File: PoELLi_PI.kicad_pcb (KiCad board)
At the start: 2 copper layers, 85 x 56 mm, 14 parts, among them J1 RJ45, J2 RJ45, P1 CONN_02X20

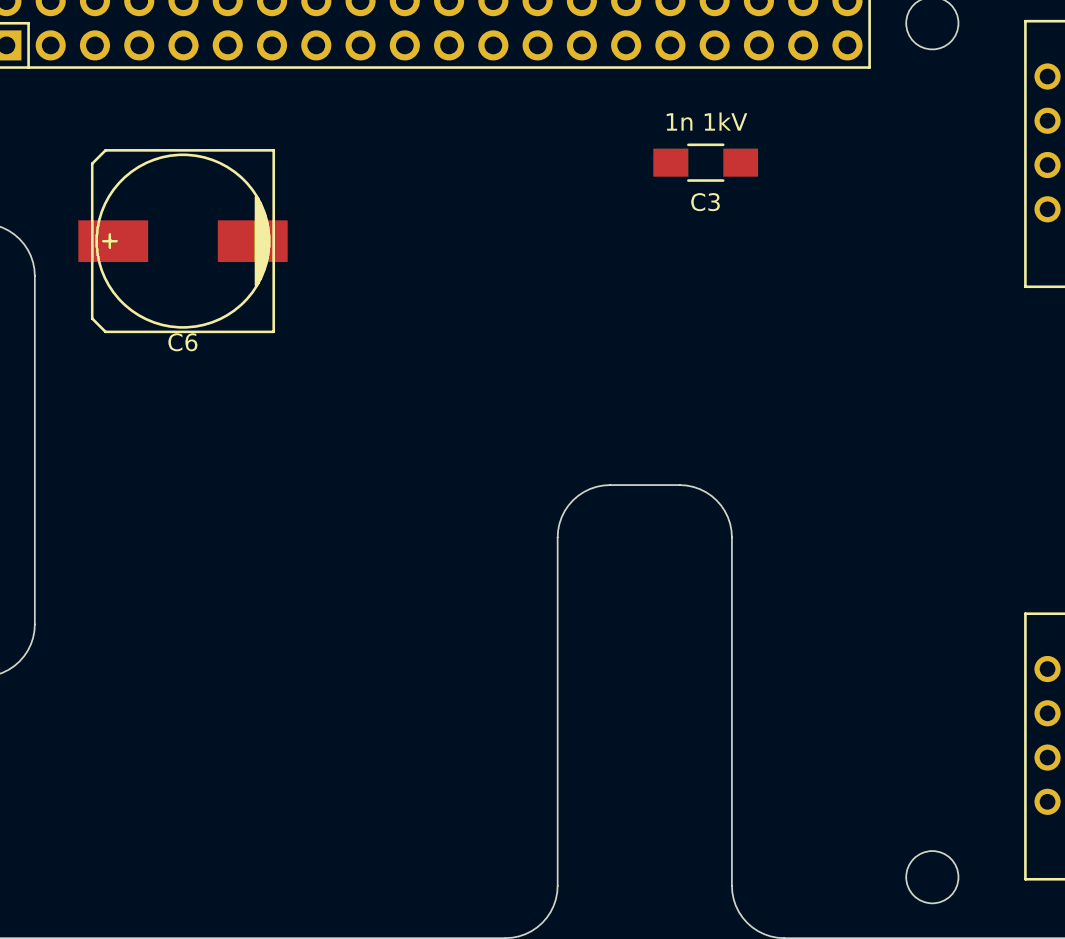
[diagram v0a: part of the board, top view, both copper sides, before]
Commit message: Add input protection diode
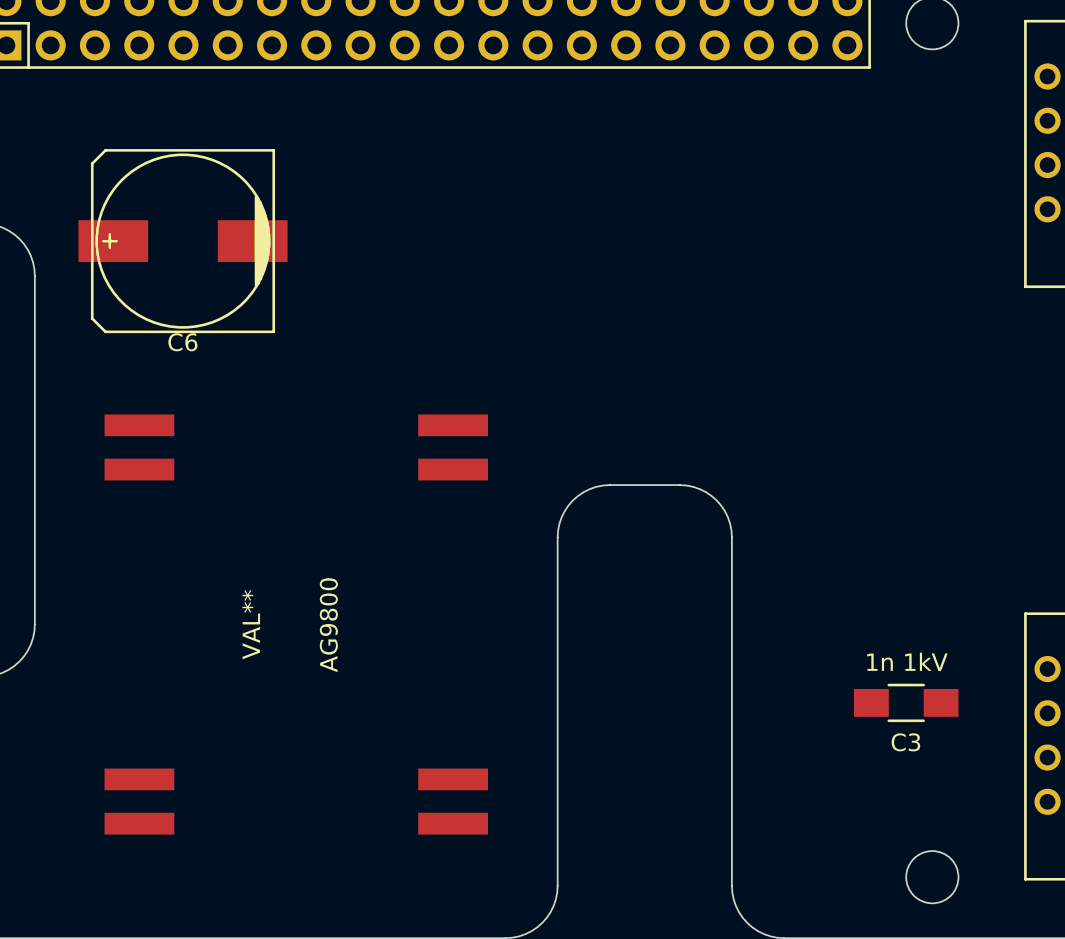
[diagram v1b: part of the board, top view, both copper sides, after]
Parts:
- added AG9800: VAL**, AG9800, F.Cu at (60.0, 70.0)
- moved C3 33.1 mm to (95.0, 74.5)
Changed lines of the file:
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@@
     (links 25)
     (no_connects 22)
-    (area 34.949999 31.949999 120.050001 88.050001)
+    (area 25.000001 25.65 194.729001 108.429)
     (thickness 1.6)
-    (drawings 40)
+    (drawings 41)
     (tracks 0)
     (zones 0)
-    (modules 14)
+    (modules 15)
     (nets 56)
   )
@@
     (mod_text_size 1 1)
     (mod_text_width 0.15)
-    (pad_size 1.5 1.5)
-    (pad_drill 0.6)
+    (pad_size 1.25 4)
+    (pad_drill 0)
     (pad_to_mask_clearance 0)
     (aux_axis_origin 0 0)
@@
     (add_net "Net-(P1-Pad8)")
   )
+  (module AG9800 (layer F.Cu)
+    (at 60 70 270)
+    (fp_text reference AG9800 (at 0 -1.905 270) (layer F.SilkS)
+      (effects (font (size 1 1) (thickness 0.15)))
+    )
+    (fp_text value VAL** (at 0 2.54 270) (layer F.SilkS)
+      (effects (font (size 1 1) (thickness 0.15)))
+    )
+    (pad 8 smd rect (at -11.43 -9 270) (size 1.25 4) (layers F.Cu F.Paste F.Mask))
+    (pad 7 smd rect (at -8.89 -9 270) (size 1.25 4) (layers F.Cu F.Paste F.Mask))
+    (pad 5 smd rect (at 11.43 -9 270) (size 1.25 4) (layers F.Cu F.Paste F.Mask))
+    (pad 6 smd rect (at 8.89 -9 270) (size 1.25 4) (layers F.Cu F.Paste F.Mask))
+    (pad 3 smd rect (at 8.89 9 270) (size 1.25 4) (layers F.Cu F.Paste F.Mask))
+    (pad 4 smd rect (at 11.43 9 270) (size 1.25 4) (layers F.Cu F.Paste F.Mask))
+    (pad 2 smd rect (at -8.89 9 270) (size 1.25 4) (layers F.Cu F.Paste F.Mask))
+    (pad 1 smd rect (at -11.43 9 270) (size 1.25 4) (layers F.Cu F.Paste F.Mask))
+  )
   (module Pin_Headers:Pin_Header_Straight_2x20 (layer F.Cu)
     (at 169 79.5)
@@
   )
   (module Capacitors_SMD:C_1206_HandSoldering (layer F.Cu)
-    (at 83.5 43.5 180)
+    (at 95 74.5 180)
     (descr "Capacitor SMD 1206, hand soldering")
     (tags "capacitor 1206")
@@
     )
   )
+  (gr_line (start 85.5 65) (end 74.5 65) (angle 90) (layer Dwgs.User) (width 0.2))
   (dimension 29 (width 0.3) (layer Dwgs.User)
     (gr_text "29.000 mm" (at 53 27.15) (layer Dwgs.User)

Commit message: First functional version before cosmetic changes
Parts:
- removed AG9800: VAL**, AG9800
- added B2: MB110S, project_specific:TO-269AA, F.Cu at (82.5, 43.0)
- added C10: 10n, Capacitors_SMD:C_0603_HandSoldering, F.Cu at (52.5, 72.2)
- added C11: 10u, Capacitors_SMD:C_0603_HandSoldering, F.Cu at (51.0, 72.2)
- added C7: 4n7 2kV, Capacitors_SMD:C_1812_HandSoldering, F.Cu at (69.8, 54.6)
- added C8: 4n7 2kV, Capacitors_SMD:C_1812_HandSoldering, F.Cu at (62.6, 47.5)
- added C9: 4n7 2kV, Capacitors_SMD:C_1812_HandSoldering, F.Cu at (59.7, 54.6)
- added D1: SMA58, Diodes_SMD:Diode-SMA_Handsoldering, F.Cu at (71.0, 49.5)
- added D2: LED, Resistors_SMD:R_0603_HandSoldering, F.Cu at (46.8, 75.3)
- added F1: FUSE, Resistors_SMD:R_0603_HandSoldering, F.Cu at (43.2, 43.2)
- added FB1: FILTER, Resistors_SMD:R_0603_HandSoldering, F.Cu at (77.5, 55.5)
- added FB2: FILTER, Resistors_SMD:R_0603_HandSoldering, F.Cu at (75.5, 44.5)
- added FB3: FILTER, Resistors_SMD:R_0603_HandSoldering, F.Cu at (77.5, 51.5)
- added FB4: FILTER, Resistors_SMD:R_0603_HandSoldering, F.Cu at (79.5, 51.5)
- added FB5: FILTER, Resistors_SMD:R_0603_HandSoldering, F.Cu at (71.5, 44.5)
- added FB6: FILTER, Resistors_SMD:R_0603_HandSoldering, F.Cu at (71.5, 42.5)
- added FB7: FILTER, Resistors_SMD:R_0603_HandSoldering, F.Cu at (77.5, 47.5)
- added FB8: FILTER, Resistors_SMD:R_0603_HandSoldering, F.Cu at (67.0, 44.5)
- added R5: 180R, Resistors_SMD:R_0603_HandSoldering, F.Cu at (46.2, 72.2)
- added R6: 100R 250 mW, Resistors_SMD:R_0603_HandSoldering, F.Cu at (47.9, 72.2)
- added R7: 100R 250 mW, Resistors_SMD:R_0603_HandSoldering, F.Cu at (49.5, 72.2)
- added TR1: 749012011, project_specific:WE_749012011, F.Cu at (104.0, 60.0)
- added U1: AG9800, AG9800, F.Cu at (62.2, 72.4)
- B1: value MBS1 -> MB110S; footprint Pin_Headers:Pin_Header_Straight_2x20 -> project_specific:TO-269AA
- C3: value 1n 1kV -> 1n 2kV
- J1, J2: footprint Connect:RJ45_8 -> project_specific:SS-7188S-A-NF
- moved B1 89.1 mm to (82.5, 58.0), turned to 270 degrees
- moved C1 60.4 mm to (92.5, 45.5), turned to 180 degrees
- moved C2 57.1 mm to (92.5, 43.0), turned to 180 degrees
- moved R2 56.1 mm to (88.5, 43.0), turned to 180 degrees
- moved R1 53.7 mm to (88.5, 45.5), turned to 180 degrees
- moved C5 45.1 mm to (92.5, 55.5), turned to 180 degrees
- moved R4 43.9 mm to (88.5, 55.5), turned to 180 degrees
- moved C4 42.8 mm to (92.5, 58.0), turned to 180 degrees
- moved R3 41.5 mm to (88.5, 58.0), turned to 180 degrees
- moved C3 24.6 mm to (89.5, 50.5), turned to 0 degrees
- moved C6 2.33 mm to (51.5, 46.8)
- moved J1 1.13 mm to (111.8, 78.1)
- moved J2 1.12 mm to (111.8, 41.9)
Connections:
- C6 pad 1: +5V -> /AG_OUT_+
- J1 pad 1: Net-(J1-Pad1) -> /TD+
- J1 pad 2: Net-(J1-Pad2) -> /TD-
- J1 pad 3: Net-(J1-Pad3) -> /RD+
- J1 pad 6: Net-(J1-Pad6) -> /RD-
- J2 pad 1: Net-(J2-Pad1) -> /TX+
- J2 pad 2: Net-(J2-Pad2) -> /TX-
- J2 pad 3: Net-(J2-Pad3) -> /RX+
- J2 pad 6: Net-(J2-Pad6) -> /RX-
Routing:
- net /AG_IN_+: track 0.00 -> 86.8 mm, vias 0 -> 6
- net /AG_IN_-: track 0.00 -> 66.4 mm, vias 0 -> 6
- net /VIN: track 0.00 -> 35.0 mm
- net Net-(C3-Pad1): track 0.00 -> 30.3 mm, vias 0 -> 3
- net GND: track 0.00 -> 28.5 mm, vias 0 -> 5
- net /POE_A-: track 0.00 -> 28.2 mm
- net GNDD: track 0.00 -> 27.1 mm
- net /AG_OUT_+: track 0.00 -> 24.1 mm
- net /POE_B+: track 0.00 -> 23.5 mm
- net /POE_B-: track 0.00 -> 22.6 mm
- net /TD+: track 0.00 -> 20.7 mm
- net /TD-: track 0.00 -> 20.1 mm
- net /RX-: track 0.00 -> 19.6 mm
- net /RD+: track 0.00 -> 19.4 mm
- net /POE_A+: track 0.00 -> 18.5 mm
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- added copper zone on F.Cu, net +5V
- added copper zone on B.Cu, net /AG_IN_+
- added copper zone on F.Cu, net /AG_IN_+
- added copper zone on B.Cu, net /AG_IN_-
- added copper zone on F.Cu, net /AG_IN_-
- added copper zone on F.Cu, net /AG_OUT_+
- added copper zone on B.Cu, net GND
- added copper zone on F.Cu, net GND
- added copper zone on B.Cu, net GNDA
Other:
- net class Default: clearance 0.254 -> 0.199
- net class Ethernet Signal added: clearance 0.199, trace_width 0.6, via_dia 0.889, via_drill 0.635
- net class Ethernet shield added: clearance 0.399, trace_width 0.254, via_dia 0.889, via_drill 0.635
- rule trace_clearance: 0.254 -> 0.199
- rule trace_min: 0.254 -> 0.15
- rule via_min_drill: 0.508 -> 0.3
- rule via_min_size: 0.889 -> 0.6

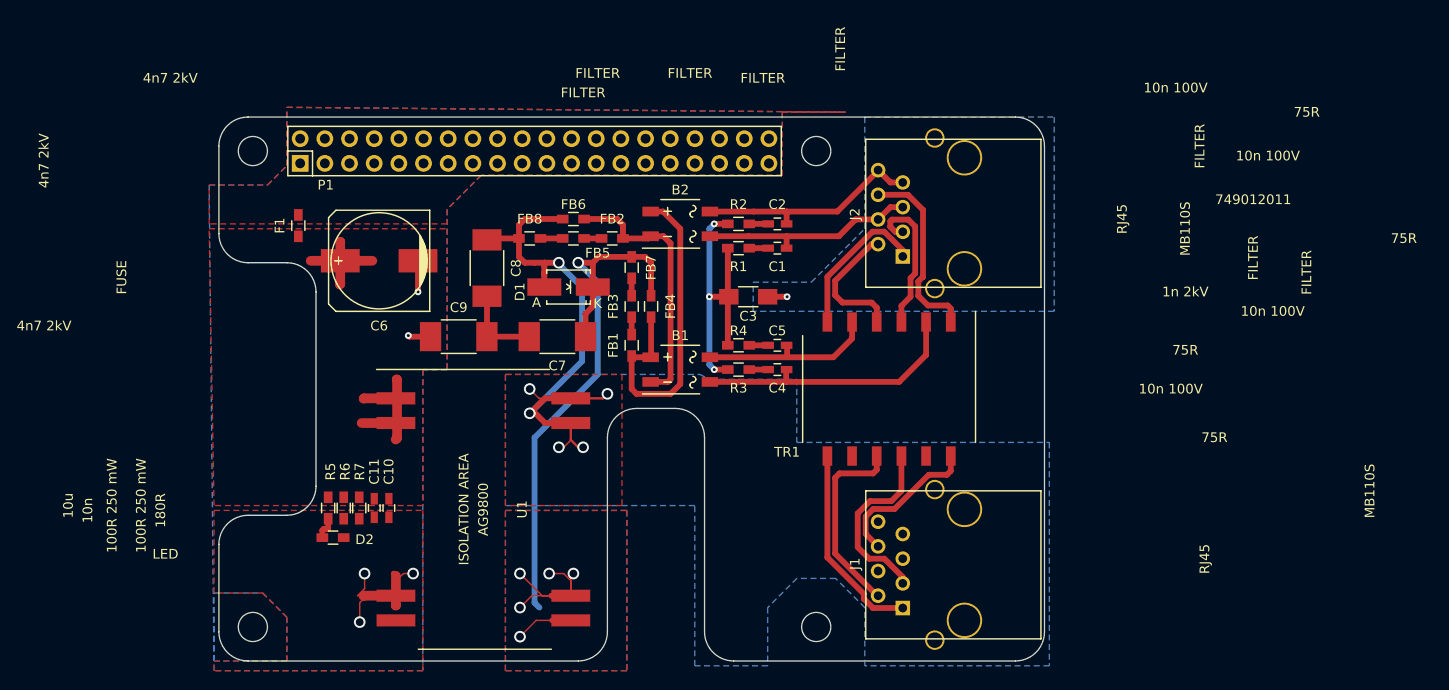
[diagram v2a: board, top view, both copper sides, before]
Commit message: First production version, with ethernet connector holes fixed
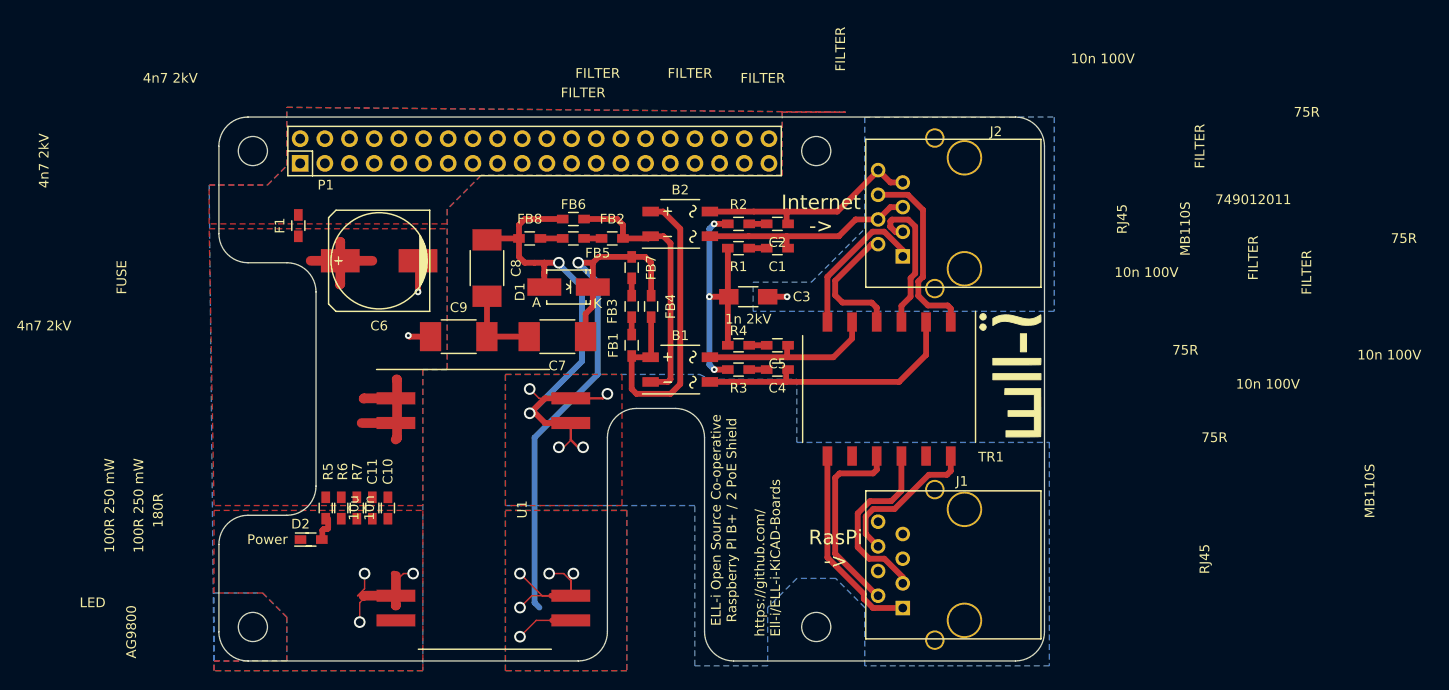
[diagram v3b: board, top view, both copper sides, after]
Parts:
- added G***: LOGO, logos:ELL-i_large, F.Cu at (116.5, 58.5)
- C1, C10, C11, C2, C4, C5: footprint Capacitors_SMD:C_0603_HandSoldering -> Resistors_SMD:R_0603_HandSoldering
- U1: footprint AG9800 -> project_specific:AG9800
- moved D2 2.26 mm to (44.5, 75.5), turned to 180 degrees
- moved R5 0.25 mm to (46.0, 72.2)
- moved R6 0.25 mm to (47.6, 72.2)
- moved R7 0.25 mm to (49.2, 72.2)
- moved C11 0.20 mm to (50.8, 72.2)
- moved C10 0.10 mm to (52.4, 72.2)
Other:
- board text added: "ELL-i Open Source Co-operative Raspberry PI B+ / 2 PoE Shield"
- board text added: "Internet ->"
- board text added: "Power"
- board text added: "RasPi ->"
- board text added: "https://github.com/ Ell-i/ELL-i-KiCAD-Boards"

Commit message: Version 1.0
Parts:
- removed FB4, FB6: FILTER, Resistors_SMD:R_0603_HandSoldering
- removed G***: LOGO, logos:ELL-i_large
- added FID1: 1, 2 mm, project_specific:Fiducial_2mm_dia, F.Cu at (38.5, 78.5)
- added FID2: 1, 2 mm, project_specific:Fiducial_2mm_dia, F.Cu at (38.5, 41.0)
- added FID3: 1, 2 mm, project_specific:Fiducial_2mm_dia, F.Cu at (117.0, 63.0)
- added LOGO102: ELL-i, logos:ELL-i_large, F.Cu at (85.0, 41.5)
- added P101: CONN_01X01, Pin_Headers:Pin_Header_Straight_1x01, F.Cu at (76.2, 83.8)
- added P102: CONN_01X01, Pin_Headers:Pin_Header_Straight_1x01, F.Cu at (76.2, 61.0)
- F1: footprint Resistors_SMD:R_0603_HandSoldering -> Resistors_SMD:R_0805_HandSoldering
- J1: value RJ45 -> RJSSE-5080; footprint project_specific:SS-7188S-A-NF -> project_specific:RJSSE-5380
- J2: value RJ45 -> RJSSE-5380; footprint project_specific:SS-7188S-A-NF -> project_specific:RJSSE-5380
- moved C3 24.9 mm to (112.8, 59.5), turned to 90 degrees
- moved R2 23.9 mm to (106.0, 59.2), turned to 0 degrees
- moved D1 23.1 mm to (75.2, 72.2), turned to 270 degrees
- moved R1 21.2 mm to (106.0, 57.5), turned to 0 degrees
- moved R4 18.9 mm to (106.0, 62.8), turned to 0 degrees
- moved C2 18.8 mm to (102.0, 59.2), turned to 0 degrees
- moved R3 17.8 mm to (106.0, 61.0), turned to 0 degrees
- moved C1 15.3 mm to (102.0, 57.5), turned to 0 degrees
- moved TR1 13.5 mm to (90.5, 60.0)
- moved B1 13.5 mm to (72.5, 49.0)
- moved C5 12.0 mm to (102.0, 62.8), turned to 0 degrees
- moved B2 10.0 mm to (72.5, 44.0)
- moved C4 9.96 mm to (102.0, 61.0), turned to 0 degrees
- moved FB7 9.06 mm to (78.5, 56.5), turned to 180 degrees
- moved FB2 8.63 mm to (67.5, 47.8), turned to 90 degrees
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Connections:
- B1 pad 2: /POE_A- -> /POE_A+
- B1 pad 4: /POE_A+ -> /POE_A-
- B2 pad 2: /POE_B- -> /POE_B+
- B2 pad 4: /POE_B+ -> /POE_B-
- P1 pad 1: +3V3 -> Net-(P1-Pad1)
- P1 pad 17: +3V3 -> Net-(P1-Pad17)
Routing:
- net /POE_A+: track 18.5 -> 55.2 mm, vias 0 -> 2
- net /POE_B-: track 22.6 -> 59.1 mm, vias 0 -> 2
- net /AG_IN_+: track 86.8 -> 54.7 mm, vias 6 -> 5
- net /POE_B+: track 23.5 -> 51.3 mm, vias 0 -> 2
- net GNDA: track 2.00 -> 21.3 mm, vias 1 -> 6
- net /POE_A-: track 28.2 -> 47.1 mm, vias 0 -> 2
- net /VIN: track 35.0 -> 16.2 mm
- net GNDD: track 27.1 -> 13.1 mm
- net Net-(C3-Pad1): track 30.3 -> 16.6 mm, vias 3 -> 0
- net /TX+: track 15.8 -> 27.3 mm
- net Net-(J1-Pad9): track 0.00 -> 11.4 mm
- net /AG_IN_-: track 66.4 -> 57.3 mm
- net /TX-: track 13.8 -> 22.2 mm
- net /RD-: track 15.8 -> 21.7 mm
- net /RD+: track 19.4 -> 23.5 mm
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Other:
- outline, holes or cut-outs redrawn
- board text added: "1A holding"
- board text added: "Optional 100R 1/4 W"
- board text added: "PoE Switch"
- board text added: "RasPi"
- board text added: "Raspberry Pi B+/2 PoE Shield"
- board text added: "Raw PoE +"
- board text added: "Raw PoE -"
- board text removed: "ELL-i Open Source Co-operative Raspberry PI B+ / 2 PoE Shield"
- board text removed: "Internet ->"
- board text removed: "RasPi ->"

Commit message: 1.0
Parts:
- added D3: TVS, Diodes_SMD:SOD-323, F.Cu at (100.5, 68.2)
- added D4: TVS, Diodes_SMD:SOD-323, F.Cu at (89.3, 70.5)
- added LOGO101: OPEN_HARDWARE_1, Symbols:Symbol_OSHW-Logo_SilkScreen, F.Cu at (96.3, 41.9)
- added P2: CONN_01X02, Pin_Headers:Pin_Header_Straight_1x02, F.Cu at (47.0, 55.2)
- added R8: R, Resistors_SMD:R_0603_HandSoldering, F.Cu at (48.3, 80.4)
- added R9: R, Resistors_SMD:R_0603_HandSoldering, F.Cu at (48.3, 84.6)
- moved U1 0.93 mm to (62.5, 71.5)
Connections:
- U1 pad 4: Net-(U1-Pad4) -> /ADJ
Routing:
- net /AG_OUT+: track 0.00 -> 14.2 mm, vias 0 -> 2
- net /AG_OUT_+: track 24.1 -> 10.8 mm
- net /AG_IN_-: track 57.3 -> 44.0 mm
- net /RD+: track 23.5 -> 33.6 mm
- net /ADJ: track 0.00 -> 7.46 mm
- net GND: track 28.5 -> 34.4 mm, vias 5 -> 8
- net /AG_IN_+: track 54.7 -> 53.8 mm, vias 5 -> 6
- net /TD+: track 21.1 -> 21.6 mm
- net (no net): vias 0 -> 2
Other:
- board text added: "+"
- board text added: "-"
- board text added: "1A1"
- board text added: "Adjust"
- board text added: "DC out"
- board text added: "Down"
- board text added: "Raspberry Pi PoE HAT for B+/2"
- board text added: "Up"
- board text removed: "1A holding"
- board text removed: "Raspberry Pi B+/2 PoE Shield"
